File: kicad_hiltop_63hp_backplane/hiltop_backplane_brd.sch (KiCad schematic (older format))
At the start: 13 parts

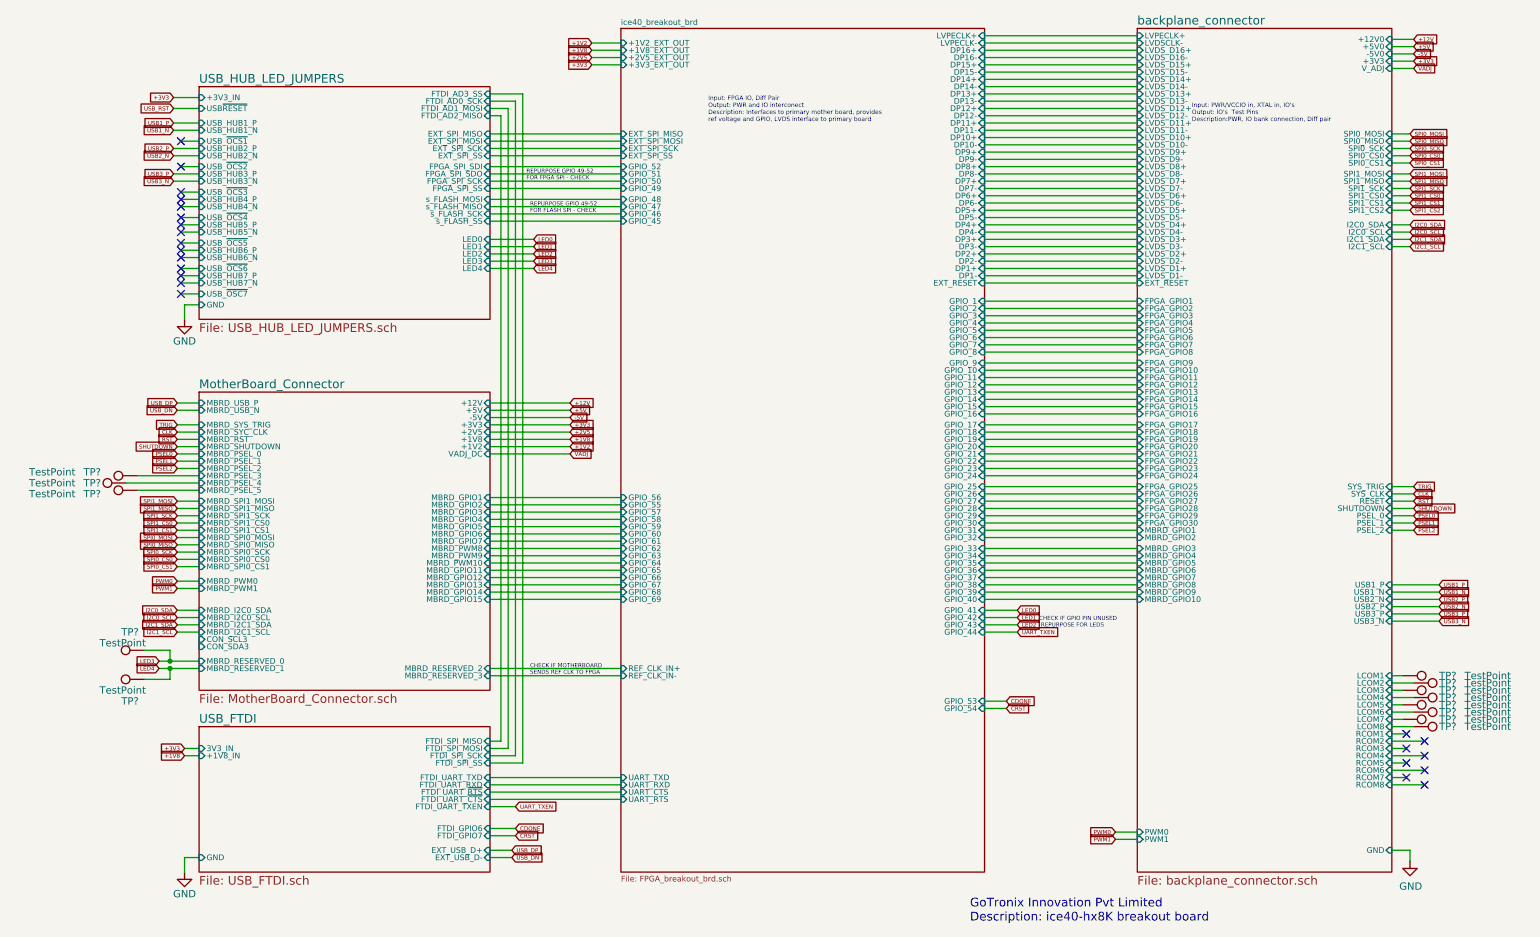
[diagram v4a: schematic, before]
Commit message: Schematic updated to reflect USB logic and Global nets changed to local nets, renamed signals in motherboard connector
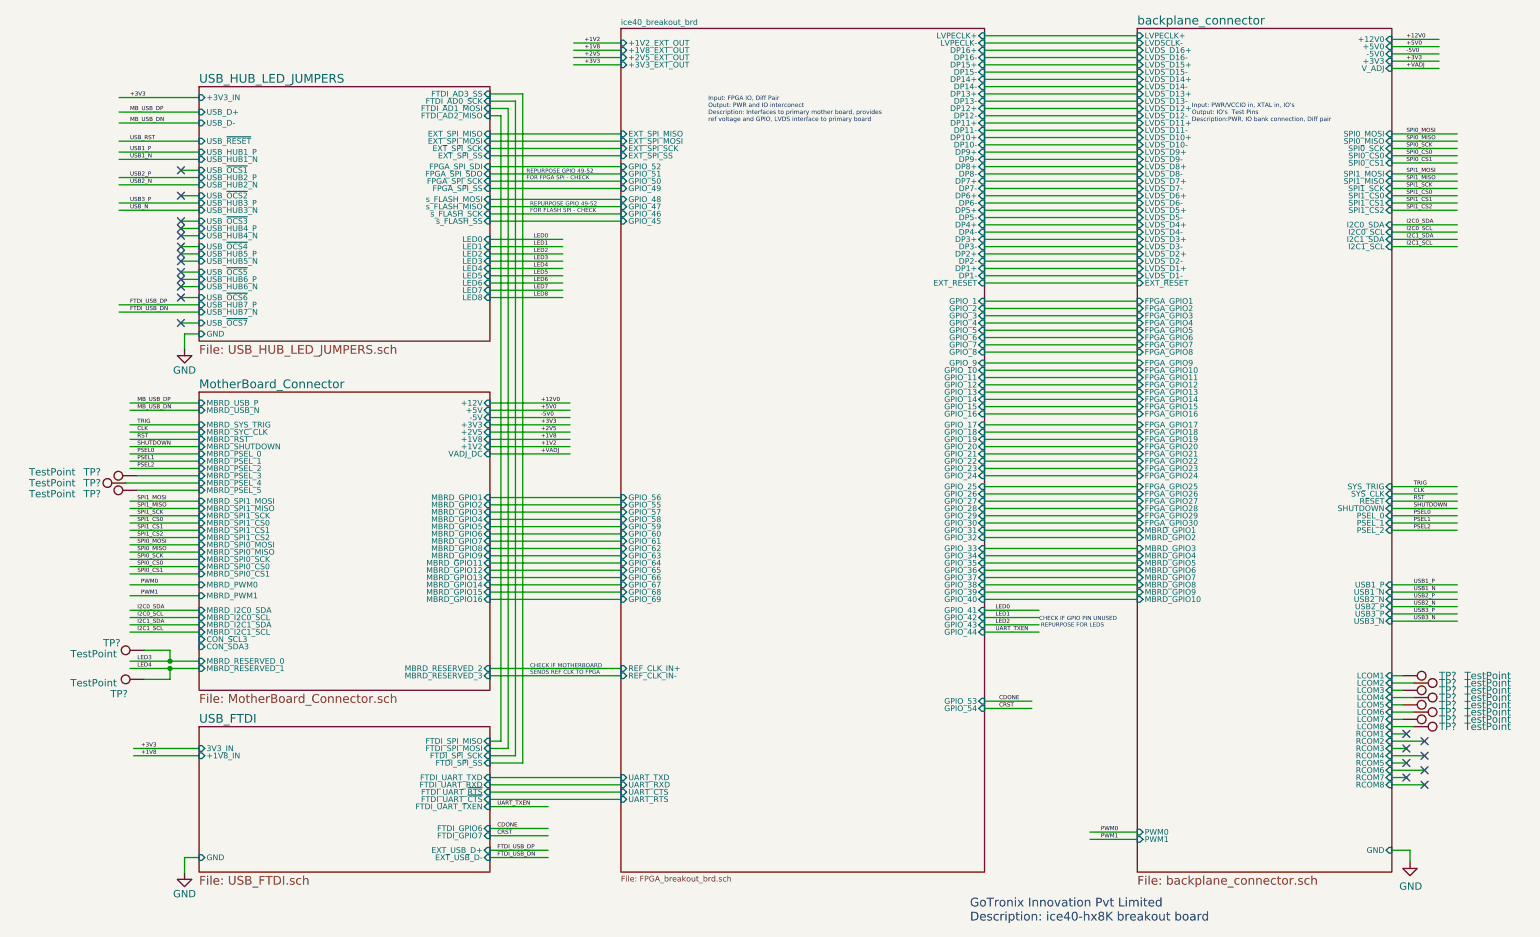
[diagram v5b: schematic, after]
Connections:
- net labels added: +12V0, +5V0, +VADJ, -5V0, FTDI_USB_DN, FTDI_USB_DP, LED5, LED6, LED7, LED8, MB_USB_DN, MB_USB_DP, USB_N
- net labels removed: +12V, +5V, -5V, USB_DN, USB_DP, VADJ
- wire segments 266 -> 273
- no-connect marks 23 -> 21

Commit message: lables connected to end of net, each component mapped to footprint, working on reducing error
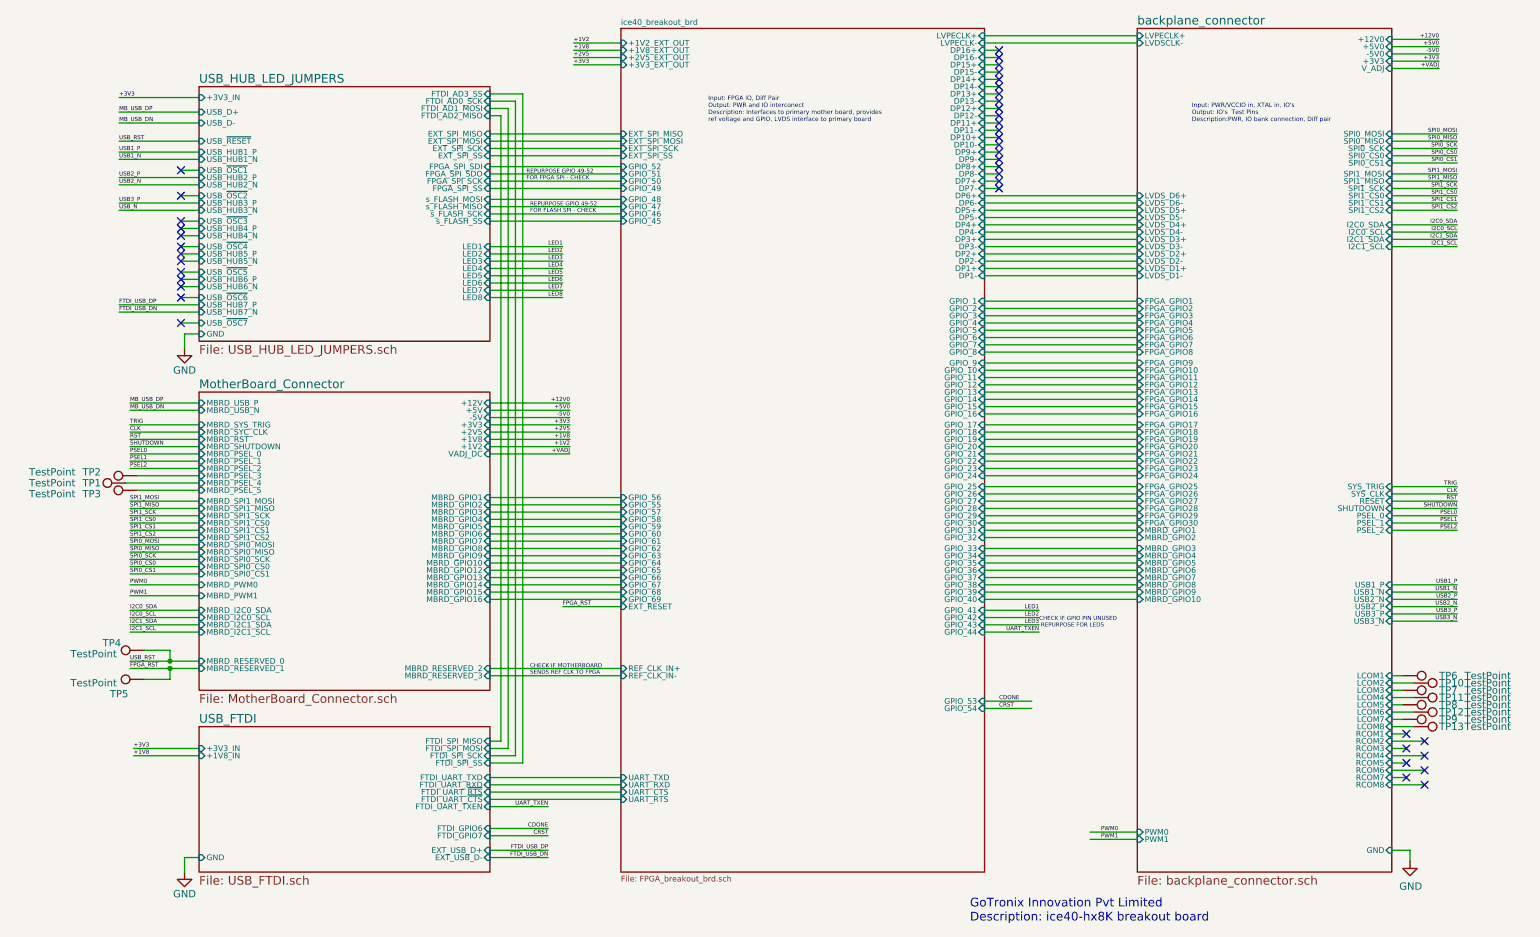
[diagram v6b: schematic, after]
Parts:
- TP1, TP10, TP11, TP12, TP13, TP2, TP3, TP4, TP5, TP6, TP7, TP8, TP9: renamed from TP?; footprint (none) -> TestPoint:TestPoint_Pad_D1.0mm
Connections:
- net labels added: FPGA_RST
- net labels removed: LED0
- wire segments 273 -> 272
- no-connect marks 21 -> 41

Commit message: schematic error reduced and footprint mapped
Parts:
- added R82, R83: DNP, symbol device:R
- added TP16: L4, symbol Connector:TestPoint
- added TP17: L6, symbol Connector:TestPoint
- added TP18: L8, symbol Connector:TestPoint
- added TP19: L5, symbol Connector:TestPoint
- added TP20: L7, symbol Connector:TestPoint
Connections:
- net LED4: now also TP16.1
- net LED5: now also TP19.1
- net LED6: now also TP17.1
- net LED7: now also TP20.1
- net LED8: now also TP18.1
- net MotherBoard_Connector/MBRD_RESERVED_2: now also R82.2
- net MotherBoard_Connector/MBRD_RESERVED_3: now also R83.2
- new net ice40_breakout_brd/REF_CLK_IN+: R82.1
- new net ice40_breakout_brd/REF_CLK_IN-: R83.1

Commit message: first pass schematic placement
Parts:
- R82, R83: footprint (none) -> Resistor_SMD:R_0402_1005Metric
- TP16, TP17, TP18, TP19, TP20: footprint (none) -> TestPoint:TestPoint_Pad_D1.0mm
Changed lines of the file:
@@
 F 0 "R82" V 4150 4800 50  0000 C CNN
 F 1 "DNP" V 4200 4950 50  0000 C CNN
-F 2 "" V 4130 4950 50  0001 C CNN
+F 2 "Resistor_SMD:R_0402_1005Metric" V 4130 4950 50  0001 C CNN
 F 3 "" H 4200 4950 50  0001 C CNN
 	1    4200 4950
@@
 F 0 "R83" V 4150 4900 50  0000 C CNN
 F 1 "DNP" V 4200 5050 50  0000 C CNN
-F 2 "" V 4130 5050 50  0001 C CNN
+F 2 "Resistor_SMD:R_0402_1005Metric" V 4130 5050 50  0001 C CNN
 F 3 "" H 4200 5050 50  0001 C CNN
 	1    4200 5050
@@
 F 0 "TP16" V 4525 2125 50  0000 L CNN
 F 1 "L4" V 4525 2350 50  0000 L CNN
-F 2 "" H 4400 2250 50  0001 C CNN
+F 2 "TestPoint:TestPoint_Pad_D1.0mm" H 4400 2250 50  0001 C CNN
 F 3 "~" H 4400 2250 50  0001 C CNN
 	1    4200 2250
@@
 F 0 "TP19" V 4625 2175 50  0000 L CNN
 F 1 "L5" V 4625 2400 50  0000 L CNN
-F 2 "" H 4475 2300 50  0001 C CNN
+F 2 "TestPoint:TestPoint_Pad_D1.0mm" H 4475 2300 50  0001 C CNN
 F 3 "~" H 4475 2300 50  0001 C CNN
 	1    4275 2300
@@
 F 0 "TP17" V 4575 2225 50  0000 L CNN
 F 1 "L6" V 4575 2450 50  0000 L CNN
-F 2 "" H 4400 2350 50  0001 C CNN
+F 2 "TestPoint:TestPoint_Pad_D1.0mm" H 4400 2350 50  0001 C CNN
 F 3 "~" H 4400 2350 50  0001 C CNN
 	1    4200 2350
@@
 F 0 "TP20" V 4675 2275 50  0000 L CNN
 F 1 "L7" V 4675 2500 50  0000 L CNN
-F 2 "" H 4475 2400 50  0001 C CNN
+F 2 "TestPoint:TestPoint_Pad_D1.0mm" H 4475 2400 50  0001 C CNN
 F 3 "~" H 4475 2400 50  0001 C CNN
 	1    4275 2400
@@
 F 0 "TP18" V 4625 2325 50  0000 L CNN
 F 1 "L8" V 4625 2550 50  0000 L CNN
-F 2 "" H 4400 2450 50  0001 C CNN
+F 2 "TestPoint:TestPoint_Pad_D1.0mm" H 4400 2450 50  0001 C CNN
 F 3 "~" H 4400 2450 50  0001 C CNN
 	1    4200 2450
